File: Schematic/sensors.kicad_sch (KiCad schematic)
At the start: 17 parts, among them IC4 ICM-42688-P, IC5 MPU-6500, U5 SPL06-001, U7 QMC5883L

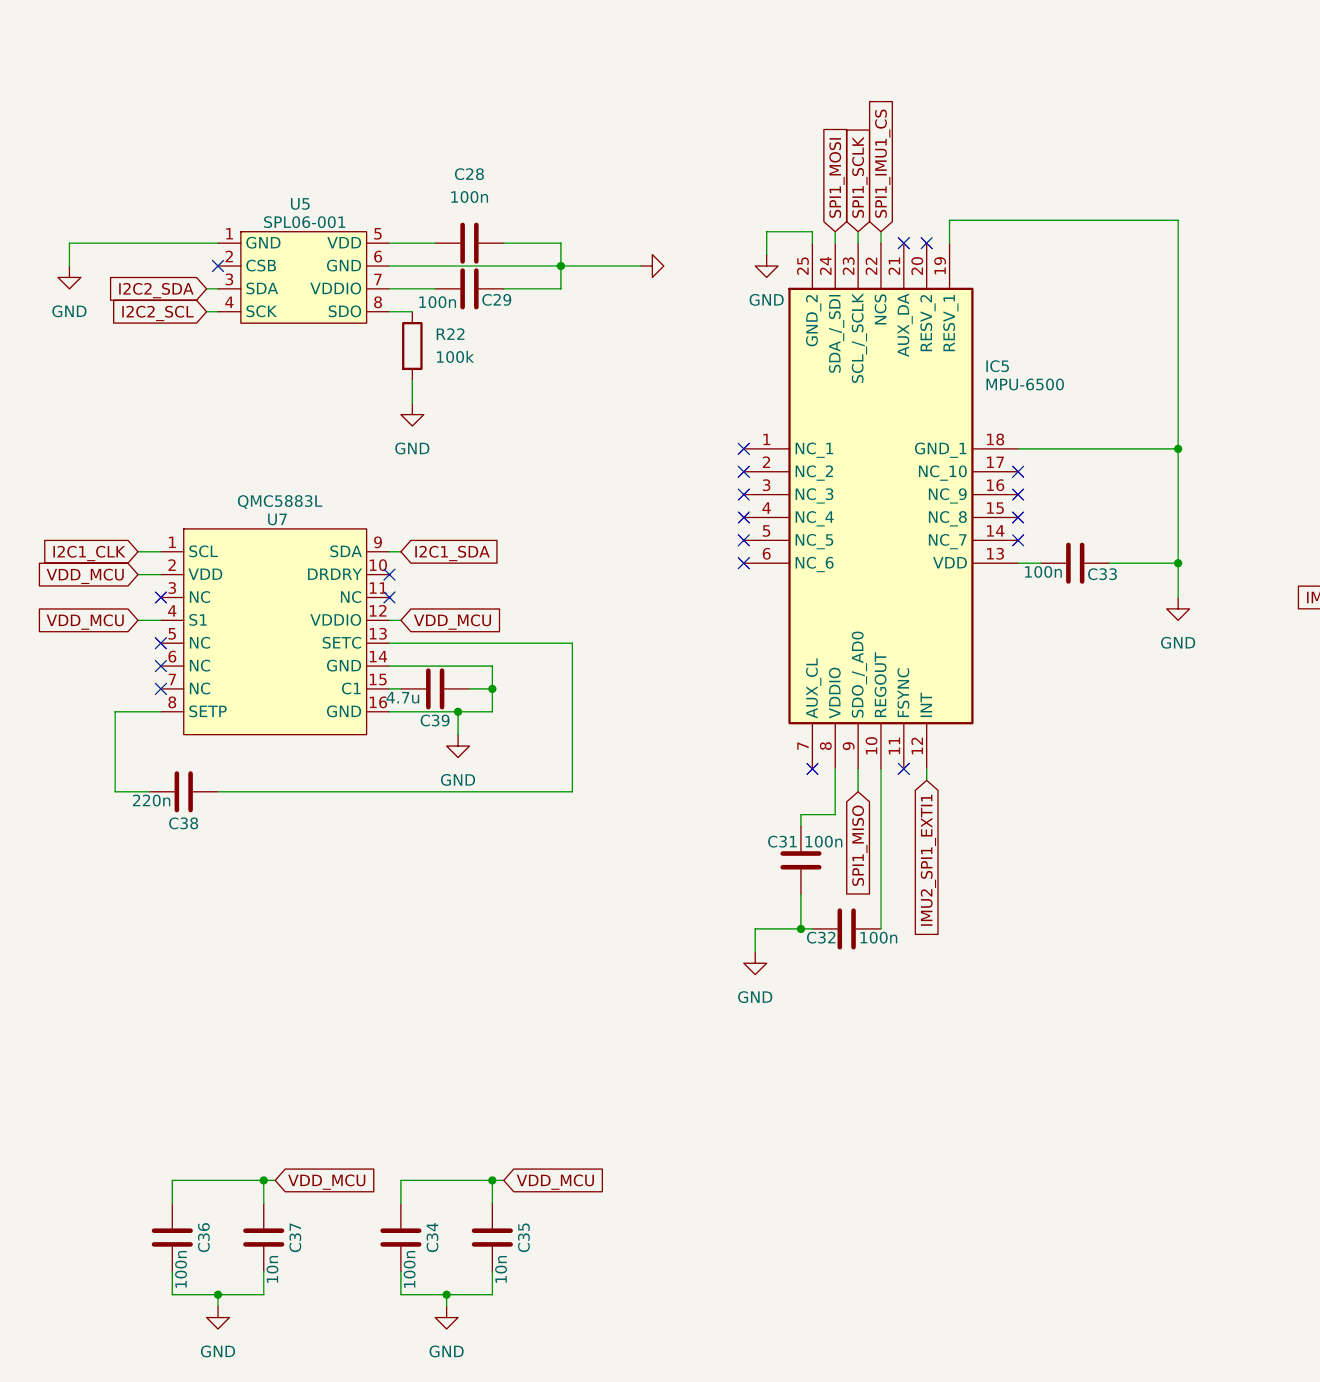
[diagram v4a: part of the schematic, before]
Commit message: Refactor schematic files and update component placements
- Adjusted component positions in osd.kicad_sch for better layout.
- Added new junctions and wires in rf_rx.kicad_sch to improve connectivity.
- Introduced additional junctions and wires in sensors.kicad_sch for enhanced signal routing.
- Removed outdated backup file fch7-2025-11-18_191836.zip and added new backup fch7-2025-11-27_202230.zip.
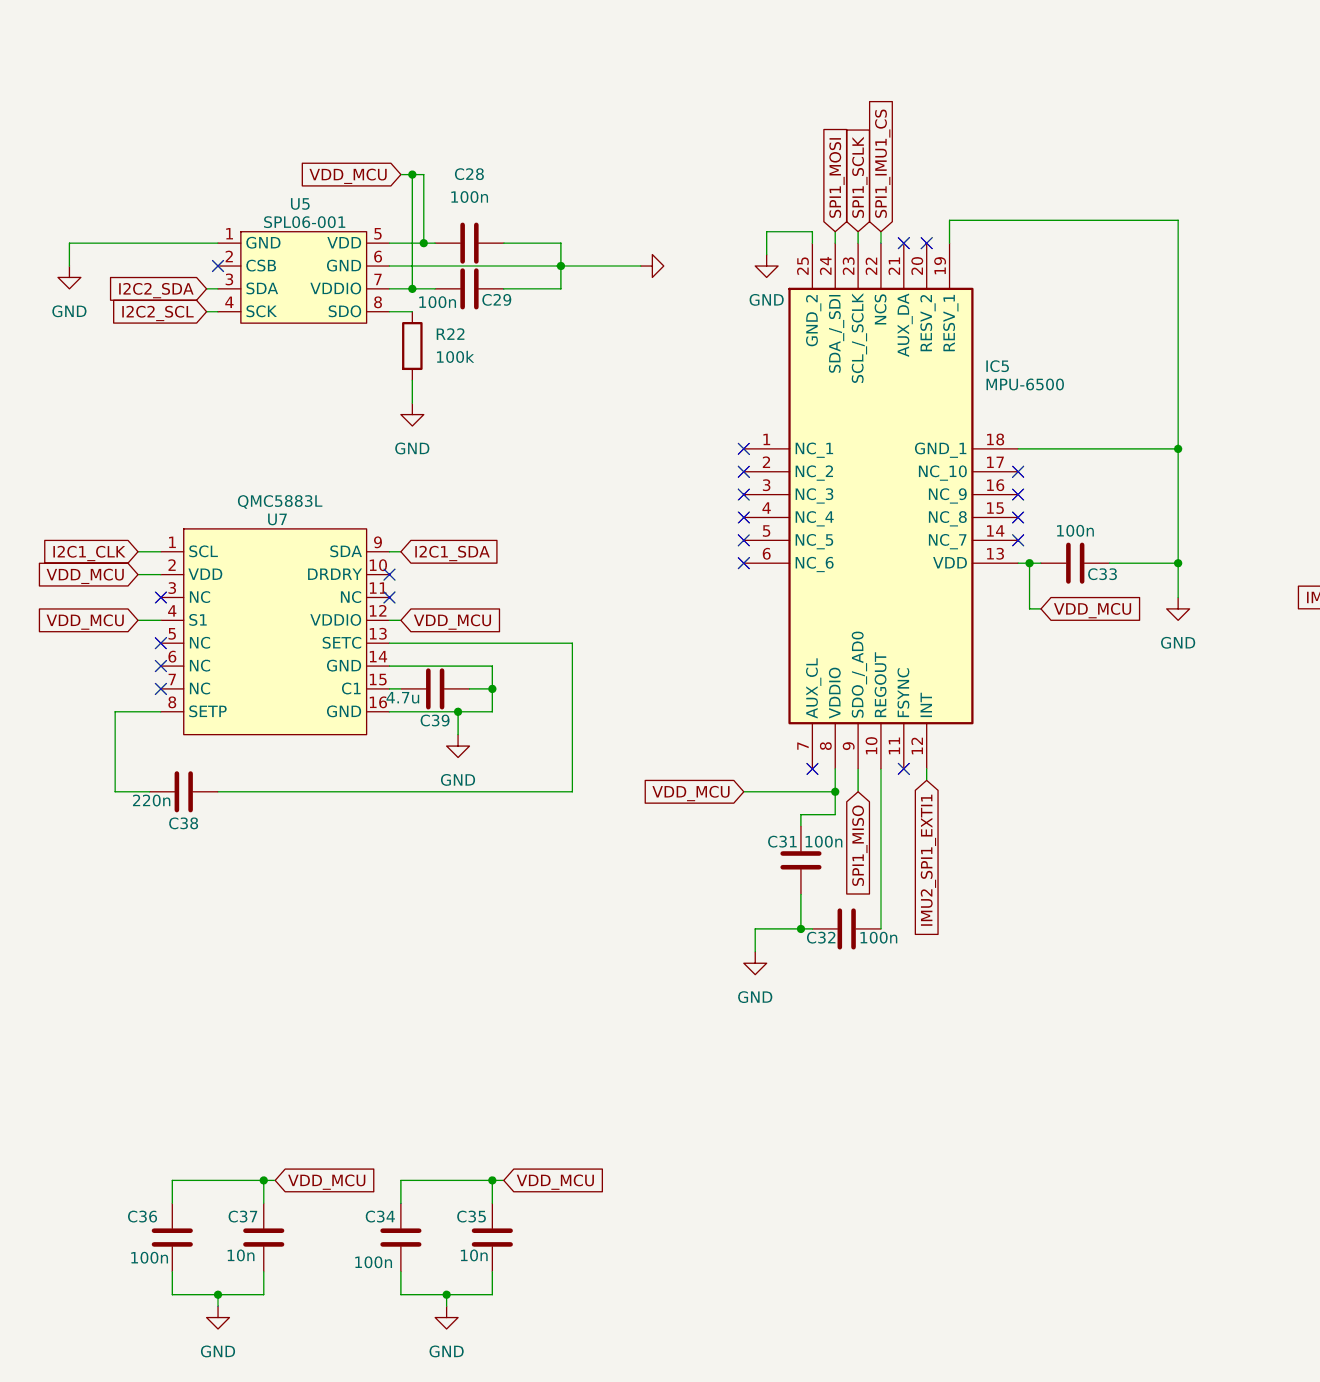
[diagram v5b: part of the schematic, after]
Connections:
- net VDD_MCU: now also C28.1, C29.1, C31.2, C33.1, IC5.13 (VDD), IC5.8 (VDDIO), U5.5 (VDD), U5.7 (VDDIO)
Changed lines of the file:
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@@
 	)
 	(junction
+		(at 146.05 76.2)
+		(diameter 0)
+		(color 0 0 0 0)
+	)
+	(junction
 		(at 162.56 63.5)
 		(diameter 0)
@@
 	)
 	(junction
+		(at 78.74 40.64)
+		(diameter 0)
+		(color 0 0 0 0)
+	)
+	(junction
 		(at 60.96 144.78)
 		(diameter 0)
@@
 	)
 	(junction
+		(at 124.46 101.6)
+		(diameter 0)
+		(color 0 0 0 0)
+	)
+	(junction
 		(at 82.55 92.71)
 		(diameter 0)
@@
 	)
 	(junction
+		(at 77.47 33.02)
+		(diameter 0)
+		(color 0 0 0 0)
+	)
+	(junction
+		(at 77.47 45.72)
+		(diameter 0)
+		(color 0 0 0 0)
+	)
+	(junction
 		(at 86.36 144.78)
 		(diameter 0)
@@
 	(wire
 		(pts
-			(xy 144.78 76.2) (xy 147.32 76.2)
+			(xy 144.78 76.2) (xy 146.05 76.2)
+		)
+		(stroke
+			(width 0)
+			(type default)
+		)
+	)
+	(wire
+		(pts
+			(xy 77.47 45.72) (xy 80.01 45.72)
 		)
 		(stroke
@@
 	(wire
 		(pts
+			(xy 124.46 101.6) (xy 124.46 104.14)
+		)
+		(stroke
+			(width 0)
+			(type default)
+		)
+	)
+	(wire
+		(pts
 			(xy 121.92 116.84) (xy 120.65 116.84)
 		)
@@
 	(wire
 		(pts
+			(xy 78.74 40.64) (xy 80.01 40.64)
+		)
+		(stroke
+			(width 0)
+			(type default)
+		)
+	)
+	(wire
+		(pts
 			(xy 121.92 40.64) (xy 121.92 39.37)
 		)
@@
 	(wire
 		(pts
-			(xy 74.93 45.72) (xy 80.01 45.72)
+			(xy 74.93 45.72) (xy 77.47 45.72)
 		)
 		(stroke
@@
 	(wire
 		(pts
+			(xy 78.74 33.02) (xy 78.74 40.64)
+		)
+		(stroke
+			(width 0)
+			(type default)
+		)
+	)
+	(wire
+		(pts
 			(xy 191.77 77.47) (xy 191.77 76.2)
 		)
@@
 	(wire
 		(pts
+			(xy 76.2 33.02) (xy 77.47 33.02)
+		)
+		(stroke
+			(width 0)
+			(type default)
+		)
+	)
+	(wire
+		(pts
 			(xy 162.56 63.5) (xy 162.56 76.2)
 		)
@@
 	(wire
 		(pts
+			(xy 114.3 101.6) (xy 124.46 101.6)
+		)
+		(stroke
+			(width 0)
+			(type default)
+		)
+	)
+	(wire
+		(pts
 			(xy 76.2 144.78) (xy 76.2 147.32)
 		)
@@
 	(wire
 		(pts
-			(xy 74.93 40.64) (xy 80.01 40.64)
+			(xy 74.93 40.64) (xy 78.74 40.64)
 		)
 		(stroke
@@
 	(wire
 		(pts
-			(xy 124.46 99.06) (xy 124.46 104.14)
+			(xy 124.46 99.06) (xy 124.46 101.6)
 		)
 		(stroke
@@
 	(wire
 		(pts
+			(xy 146.05 81.28) (xy 146.05 76.2)
+		)
+		(stroke
+			(width 0)
+			(type default)
+		)
+	)
+	(wire
+		(pts
 			(xy 87.63 45.72) (xy 93.98 45.72)
 		)
@@
 	(wire
 		(pts
+			(xy 146.05 76.2) (xy 147.32 76.2)
+		)
+		(stroke
+			(width 0)
+			(type default)
+		)
+	)
+	(wire
+		(pts
 			(xy 54.61 48.26) (xy 55.88 48.26)
 		)
@@
 	(wire
 		(pts
+			(xy 77.47 33.02) (xy 78.74 33.02)
+		)
+		(stroke
+			(width 0)
+			(type default)
+		)
+	)
+	(wire
+		(pts
 			(xy 93.98 43.18) (xy 102.87 43.18)
 		)
@@
 	(wire
 		(pts
+			(xy 77.47 33.02) (xy 77.47 45.72)
+		)
+		(stroke
+			(width 0)
+			(type default)
+		)
+	)
+	(wire
+		(pts
 			(xy 243.84 102.87) (xy 243.84 100.33)
 		)
@@
 	(wire
 		(pts
+			(xy 147.32 81.28) (xy 146.05 81.28)
+		)
+		(stroke
+			(width 0)
+			(type default)
+		)
+	)
+	(wire
+		(pts
 			(xy 77.47 55.88) (xy 77.47 58.42)
 		)
@@
 	(global_label "VDD_MCU"
 		(shape input)
+		(at 147.32 81.28 0)
+		(fields_autoplaced yes)
+		(effects
+			(font
+				(size 1.27 1.27)
+			)
+			(justify left)
+		)
+		(property "Intersheetrefs" "${INTERSHEET_REFS}"
+			(at 158.9533 81.28 0)
+			(effects
+				(font
+					(size 1.27 1.27)
+				)
+				(justify left)
+				(hide yes)
+			)
+		)
+	)
+	(global_label "VDD_MCU"
+		(shape input)
 		(at 76.2 82.55 0)
 		(fields_autoplaced yes)
@@
 		)
 	)
+	(global_label "VDD_MCU"
+		(shape input)
+		(at 76.2 33.02 180)
+		(fields_autoplaced yes)
+		(effects
+			(font
+				(size 1.27 1.27)
+			)
+			(justify right)
+		)
+		(property "Intersheetrefs" "${INTERSHEET_REFS}"
+			(at 64.5667 33.02 0)
+			(effects
+				(font
+					(size 1.27 1.27)
+				)
+				(justify right)
+				(hide yes)
+			)
+		)
+	)
 	(global_label "I2C2_SCL"
 		(shape input)
@@
 		)
 	)
+	(global_label "VDD_MCU"
+		(shape input)
+		(at 114.3 101.6 180)
+		(fields_autoplaced yes)
+		(effects
+			(font
+				(size 1.27 1.27)
+			)
+			(justify right)
+		)
+		(property "Intersheetrefs" "${INTERSHEET_REFS}"
+			(at 102.6667 101.6 0)
+			(effects
+				(font
+					(size 1.27 1.27)
+				)
+				(justify right)
+				(hide yes)
+			)
+		)
+	)
 	(global_label "I2C1_SDA"
 		(shape input)
@@
 		)
 		(property "Value" "100n"
-			(at 147.574 77.216 90)
+			(at 151.13 72.644 90)
 			(effects
 				(font
@@
 		(dnp no)
 		(property "Reference" "C34"
-			(at 79.756 151.13 90)
+			(at 73.914 148.844 0)
 			(effects
 				(font
@@
 		)
 		(property "Value" "100n"
-			(at 77.216 154.686 90)
+			(at 73.152 153.924 0)
 			(effects
 				(font
@@
 		(dnp no)
 		(property "Reference" "C36"
-			(at 54.356 151.13 90)
+			(at 47.498 148.844 0)
 			(effects
 				(font
@@
 		)
 		(property "Value" "100n"
-			(at 51.816 154.686 90)
+			(at 48.26 153.416 0)
 			(effects
 				(font
@@
 		(dnp no)
 		(property "Reference" "C37"
-			(at 64.516 151.13 90)
+			(at 58.674 148.844 0)
 			(effects
 				(font
@@
 		)
 		(property "Value" "10n"
-			(at 61.976 154.686 90)
+			(at 58.42 153.162 0)
 			(effects
 				(font
@@
 		(dnp no)
 		(property "Reference" "C35"
-			(at 89.916 151.13 90)
+			(at 84.074 148.844 0)
 			(effects
 				(font
@@
 		)
 		(property "Value" "10n"
-			(at 87.376 154.686 90)
+			(at 84.328 153.162 0)
 			(effects
 				(font

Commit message: Refactor code structure for improved readability and maintainability
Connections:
- net VDD_MCU: no longer C30.1, IC4.5 (VDDIO), IC4.8 (VDD)
- new net VCC_ICM: C30.1, IC4.5 (VDDIO), IC4.8 (VDD)
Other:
- note added: "COMPASS"
- note added: "IMU1"
- note added: "IMU2"
- note added: "Pressure sensor"
- moved on the sheet: C28, C29, C30, C31, C32, C33, C34, C35, C36, C37, C38, C39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
